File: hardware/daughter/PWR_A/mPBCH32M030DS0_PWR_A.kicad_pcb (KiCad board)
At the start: 2 copper layers, 22.9 x 70.7 mm, 72 parts, among them J1 SOCK_L, J2 SOCK_R, J3 PWR_IN, J4 MOTOR, Q1 TPN1R603PL, Q10 TPN1R603PL, Q2 TPN1R603PL, Q3 TPN1R603PL, Q4 TPN1R603PL, Q5 TPN1R603PL, Q6 TPN1R603PL, Q7 TPN1R603PL, Q8 TPN1R603PL, Q9 TPN2R304PL, U2 78L05, U4 LM74700-Q1, U5 LM74700-Q1

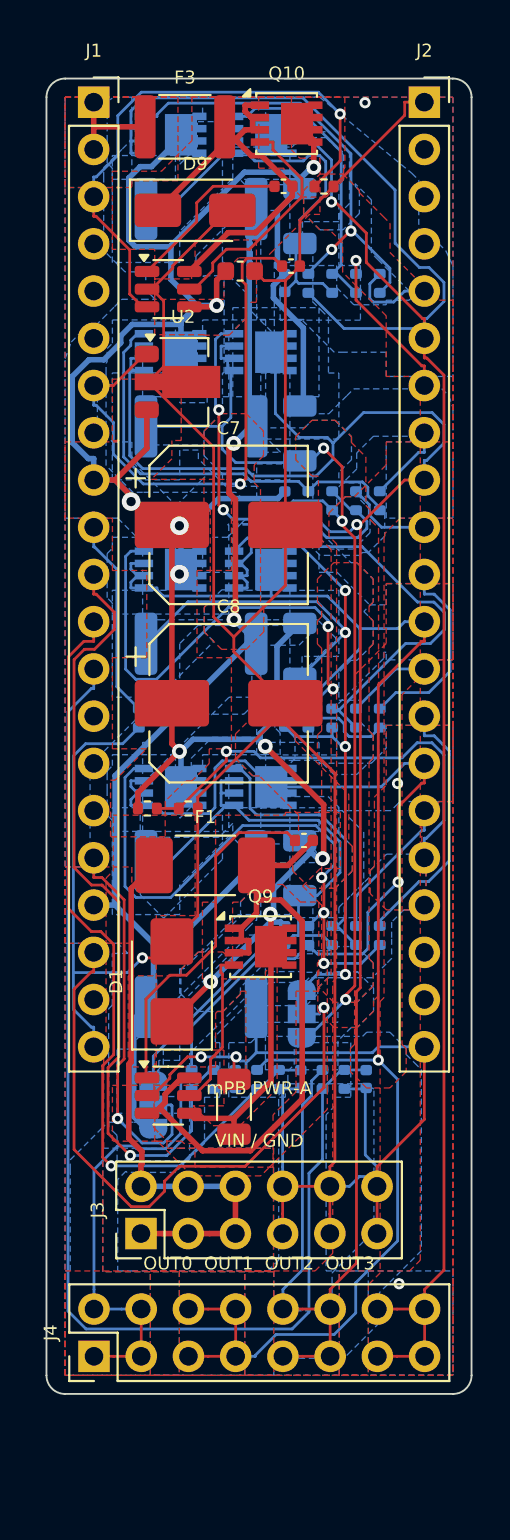
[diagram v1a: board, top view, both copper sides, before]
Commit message: 子基板 A/C: 電源の銅箔を配線前に置く再レイアウト (A 約4A/相, C 3A)
- レッグを LS/HS の縦ブロックにし, 下面 = ISH の背骨 + SRC/VBUS/SW の島,
  上面 = VBUS の帯と各相 SW の階段状の帯 (J4 は 180° 回転: OUT3 が上)
- 固定ベタは DSN では keepout (縁 0.3mm は同ネットの取り付き用) + via_keepout にして
  自動配線がベタを削らないようにした。2 段配線 (MPB_TWO_PHASE) も用意
- A: ゲート抵抗 (0805) の電極間を SW/GL が抜ける配置 (J2 の並びと FET のゲート位置の上下逆を解消)
- A/C: バルク容量は ISH 戻り (VBUS-ISH), USB 側 TVS (D9) は省略, NTC は下側へ
- 電流チェックに 1mm 平均の密度 (角の電流集中を除く) を追加
- ヒートシンクの干渉チェックは MOSFET の範囲だけに

Co-Authored-By: Claude Opus 5.5 <noreply@anthropic.com>
Claude-Session: https://claude.ai/code/session_01LENFjjhDfYjJZV1NWhB9uV
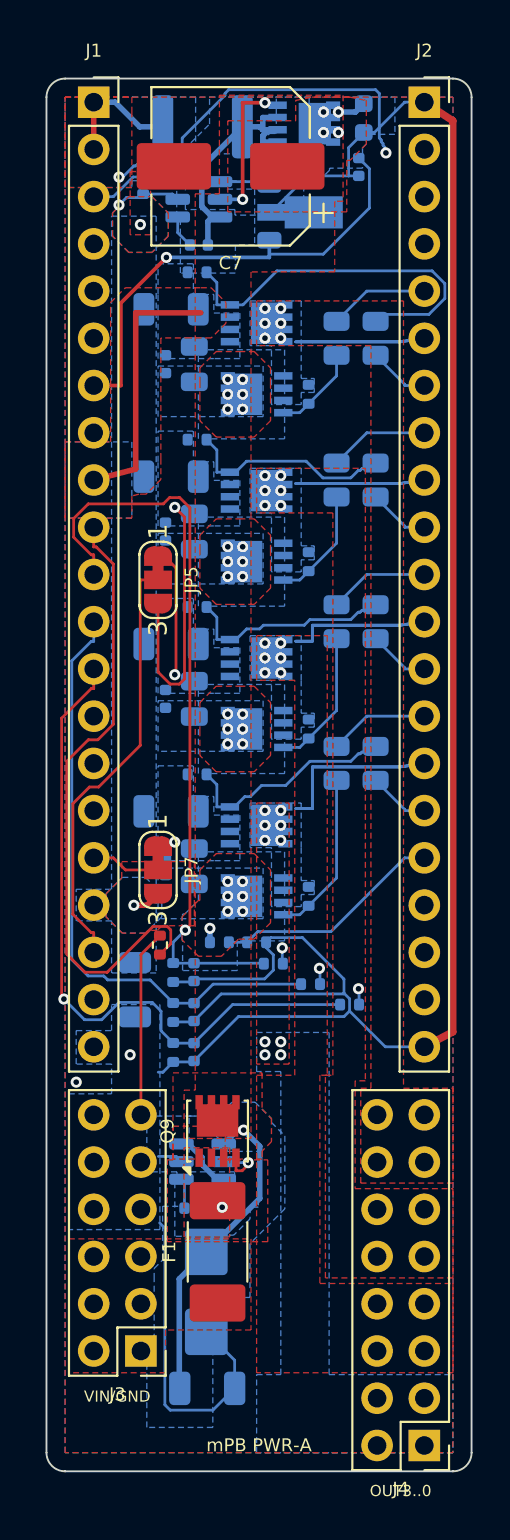
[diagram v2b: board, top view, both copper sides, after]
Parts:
- removed C8: 100uF/25V, CP_Elec_8x6.2
- removed D9: SMAJ20A, D_SMA
- C1, C3, C4, C5, C6, D1, F3, Q10, R11, R12, R6, U2, U4, U5: moved to B.Cu
- C31, C41, C51, C61: value 10uF/50V -> 10uF/25V; footprint C_1206_3216Metric -> C_0805_2012Metric
- C7: value 100uF/25V -> 150uF/25V
- F1: value 10A -> 7A
- JP5, JP7, TH1: moved to F.Cu
- R30, R32, R40, R42, R50, R52, R60, R62: footprint R_0402_1005Metric -> R_0805_2012Metric
- R34, R44, R54, R64, R70: value 10mR 1% 2W -> 10mR 1% 0.5W; footprint R_2512_6332Metric -> R_1206_3216Metric
- moved JP5 24.6 mm to (6.00, 27.0)
- moved F1 20.8 mm to (9.20, 63.1), turned to 90 degrees
- moved C5 20.6 mm to (7.90, 60.8)
- moved C7 19.3 mm to (9.90, 4.72), turned to 180 degrees
- moved J4 18.4 mm to (20.3, 73.5), turned to 180 degrees
- moved D1 16.8 mm to (8.59, 65.2), turned to -90 degrees
- moved C1 15.2 mm to (8.64, 70.4), turned to 0 degrees
- moved Q7 14.7 mm to (11.3, 17.0), turned to 180 degrees
- moved JP7 12.6 mm to (6.00, 42.6)
- moved TH1 12.3 mm to (6.10, 46.6), turned to 90 degrees
- moved Q5 12.2 mm to (11.3, 26.0), turned to 180 degrees
- moved R33 11.3 mm to (8.10, 37.4), turned to 180 degrees
- moved U2 11.3 mm to (13.9, 7.20)
- moved C3 10.6 mm to (17.1, 2.12), turned to -90 degrees
- moved Q9 10.2 mm to (9.20, 56.6), turned to 90 degrees
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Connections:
- C7 pad 2: GND -> ISH
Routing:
- net VBUS: track 152.7 -> 40.9 mm, vias 10 -> 30
- net SW3: track 114.2 -> 13.9 mm, vias 2 -> 6
- net SW2: track 109.6 -> 14.7 mm, vias 1 -> 7
- net SW1: track 89.6 -> 16.4 mm, vias 1 -> 7
- net ISH: track 64.8 -> 1.55 mm
- net SW0: track 71.8 -> 19.2 mm, vias 2 -> 11
- net SRC1: track 54.1 -> 7.01 mm, vias 4 -> 1
- net SRC2: track 55.2 -> 14.9 mm, vias 3 -> 1
- net SRC0: track 35.8 -> 0.98 mm, vias 0 -> 1
- net GND: track 193.5 -> 159.5 mm, vias 4 -> 5
- net VIN: track 30.8 -> 0.00 mm
- net VIN_F: track 36.2 -> 5.87 mm, vias 0 -> 1
- net BEMF_W: track 64.0 -> 36.7 mm, vias 0 -> 1
- net PD_PWR_EN: track 29.7 -> 5.16 mm, vias 1 -> 0
- net SRC3: track 24.3 -> 0.00 mm
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- added copper zone on B.Cu, net USB_VBUS_P
- added copper zone on B.Cu, net VIN_F
- removed copper zone on F.Cu, net SRC1
- removed copper zone on F.Cu, net SRC2
- removed copper zone on F.Cu, net USB_VBUS_P
- removed copper zone on B.Cu, net VIN
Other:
- board size 22.9 x 70.7 mm -> 22.9 x 74.9 mm
- board text added: "OUT3..0"
- board text added: "VIN/GND"
- board text removed: "OUT0 OUT1 OUT2 OUT3"
- board text removed: "VIN / GND"

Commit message: 子基板 A/C: 電源ベタにはんだ盛り用のレジスト開口, JP5 の向きを修正
- 配線前に置く電源ベタ (VBUS/ISH/VIN/VIN_F/GND/SW*/SRC*) の上のレジストを開ける
  (ベタの塗りを 0.25mm 内側に縮めた形。銅の縁と他ネットの間はレジストを残してブリッジを防ぐ)
- JP5 を 180° 回して 1 番 (SRC1) をレッグ 1 側へ。SRC2 が ISH の背骨 (下面) を横切っていたのを解消
  (A の ISH レッグ 2/3: 4.5A → 7.9A)
- 電流容量チェック (tools/power_check): レジスト開口のはんだ厚 (MPB_SOLDER_T) を銅の厚みに換算して解く
- A: はんだ 0.3mm 盛りで全経路 5A 以上 (最小 SW 5.9A, USB 系 3A 経路 5.1A 以上)
- C: 全経路 3A 以上 (USB 帰路 GND が 3.0A で最小)

Co-Authored-By: Claude Opus 5.5 <noreply@anthropic.com>
Claude-Session: https://claude.ai/code/session_01LENFjjhDfYjJZV1NWhB9uV
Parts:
- turned JP5 to 90 degrees
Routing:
- net GND: track 159.5 -> 143.0 mm, vias 5 -> 6
- net SRC2: track 14.9 -> 2.97 mm
- net BEMF_U: track 40.2 -> 28.3 mm
- net ISB_SEL: track 23.3 -> 31.6 mm
- net NTC: track 33.5 -> 25.8 mm
- net SRC1: track 7.01 -> 4.17 mm
- net BEMF_W: track 36.7 -> 36.2 mm
- net SW1: vias 7 -> 9
- net SW3: vias 6 -> 8
- net SW2: vias 7 -> 9
- net SW0: vias 11 -> 13
